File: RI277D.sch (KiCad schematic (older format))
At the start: 8 parts, among them J1 Ribbon Cable, J2 Multiway

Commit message: version 1.2 prototype ready
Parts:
- removed J2: Multiway, Connector_PinHeader_2.54mm:PinHeader_1x06_P2.54mm_Vertical, symbol Connector_Generic:Conn_01x06
- added J2: Tape Return, Connector_Molex:Molex_KK-254_AE-6410-03A_1x03_P2.54mm_Vertical, symbol Connector_Generic:Conn_01x03
- J1: footprint Connector_PinHeader_2.54mm:PinHeader_1x10_P2.54mm_Vertical -> Connector_Molex:Molex_KK-254_AE-6410-10A_1x10_P2.54mm_Vertical
- SK1: footprint Connector_PinHeader_2.54mm:PinHeader_1x03_P2.54mm_Vertical -> Connector_Molex:Molex_KK-254_AE-6410-03A_1x03_P2.54mm_Vertical
- SK2, SK3, SK4: footprint Connector_Audio:Jack_6.35mm_Neutrik_NMJ6HCD2_Horizontal -> Cliff:CL13345
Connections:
- net at J1.1 (Pin_1): now also SK1.3 (Pin_3); no longer SK1.2 (Pin_2)
- net at J1.2 (Pin_2): now also SK1.2 (Pin_2); no longer SK1.3 (Pin_3)
- net at J1.6 (Pin_6), SK2.RN: now also J2.3 (Pin_3)
- net GND: now reaches R2.1, SK1.1 (Pin_1), SK2.S, SK2.SN, SK3.S, SK3.SN, SK4.S, SK4.SN
- net GND: now also J2.1 (Pin_1)
- net at SK2.TN: now also J2.2 (Pin_2)
- no-connect marks 0 -> 5
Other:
- note added: "SCN\nTRR\nTRT\n1 GND\n3 -\n2 +"
- note removed: "SCN\nTRR\nTRT\nSCN\n-\n+"
- moved on the sheet: SK1
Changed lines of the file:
@@
 U 1 1 5F7BCA68
 P 4200 3000
-F 0 "J1" H 4150 3600 50  0000 L CNN
-F 1 "Ribbon Cable" H 4150 3500 50  0000 L CNN
-F 2 "Connector_PinHeader_2.54mm:PinHeader_1x10_P2.54mm_Vertical" H 4200 3000 50  0001 C CNN
+F 0 "J1" H 4150 2400 50  0000 L CNN
+F 1 "Ribbon Cable" H 4300 2400 50  0000 L CNN
+F 2 "Connector_Molex:Molex_KK-254_AE-6410-10A_1x10_P2.54mm_Vertical" H 4200 3000 50  0001 C CNN
 F 3 "~" H 4200 3000 50  0001 C CNN
 	1    4200 3000
@@
 $EndComp
 $Comp
-L Connector_Generic:Conn_01x06 J2
-U 1 1 5F7C4141
-P 4200 2000
-F 0 "J2" H 4150 2400 50  0000 L CNN
-F 1 "Multiway" H 4150 2300 50  0000 L CNN
-F 2 "Connector_PinHeader_2.54mm:PinHeader_1x06_P2.54mm_Vertical" H 4200 2000 50  0001 C CNN
-F 3 "~" H 4200 2000 50  0001 C CNN
-	1    4200 2000
-	1    0    0    -1
-$EndComp
-$Comp
 L Connector_Generic:Conn_01x03 SK1
 U 1 1 5F7C5243
-P 4200 3900
-F 0 "SK1" H 4150 4200 50  0000 L CNN
-F 1 "MIC Input" H 4150 4100 50  0000 L CNN
-F 2 "Connector_PinHeader_2.54mm:PinHeader_1x03_P2.54mm_Vertical" H 4200 3900 50  0001 C CNN
-F 3 "~" H 4200 3900 50  0001 C CNN
-	1    4200 3900
+P 4200 2200
+F 0 "SK1" H 4150 2000 50  0000 L CNN
+F 1 "MIC Input" H 4350 2000 50  0000 L CNN
+F 2 "Connector_Molex:Molex_KK-254_AE-6410-03A_1x03_P2.54mm_Vertical" H 4200 2200 50  0001 C CNN
+F 3 "~" H 4200 2200 50  0001 C CNN
+	1    4200 2200
 	1    0    0    -1
 $EndComp
@@
 Connection ~ 2700 1800
 Wire Wire Line
-	2700 1800 3900 1800
+	2700 1800 3400 1800
 Wire Wire Line
 	2600 3500 2700 3500
@@
 	2700 3800 2800 3800
 Wire Wire Line
-	3600 3900 3600 3500
-Wire Wire Line
-	3600 3500 4000 3500
+	3900 3800 3900 3500
+Wire Wire Line
+	3900 3500 4000 3500
 Wire Wire Line
 	2600 2850 2900 2850
@@
 	3600 1900 4000 1900
 Wire Wire Line
-	4000 2600 3800 2600
-Wire Wire Line
-	3800 2600 3800 2300
-Wire Wire Line
-	3800 2300 4000 2300
-Wire Wire Line
-	4000 3900 3800 3900
-Wire Wire Line
-	3800 3900 3800 2600
-Connection ~ 3800 2600
-Wire Wire Line
-	3700 4000 3700 2700
-Wire Wire Line
-	3700 2200 4000 2200
-Wire Wire Line
-	4000 2700 3700 2700
+	4000 2600 3900 2600
+Wire Wire Line
+	3900 2600 3900 2300
+Wire Wire Line
+	3900 2300 4000 2300
+Wire Wire Line
+	3800 2200 4000 2200
+Wire Wire Line
+	4000 2700 3800 2700
 $Comp
 L Connector:AudioJack3_Switch SK3
@@
 F 0 "SK3" H 2382 3275 50  0000 C CNN
 F 1 "Insert" H 2382 3184 50  0000 C CNN
-F 2 "Connector_Audio:Jack_6.35mm_Neutrik_NMJ6HCD2_Horizontal" H 2400 2850 50  0001 C CNN
+F 2 "Cliff:CL13345" H 2400 2850 50  0001 C CNN
 F 3 "~" H 2400 2850 50  0001 C CNN
 	1    2400 2850
@@
 F 0 "SK4" H 2382 4125 50  0000 C CNN
 F 1 "Direct Out" H 2382 4034 50  0000 C CNN
-F 2 "Connector_Audio:Jack_6.35mm_Neutrik_NMJ6HCD2_Horizontal" H 2400 3700 50  0001 C CNN
+F 2 "Cliff:CL13345" H 2400 3700 50  0001 C CNN
 F 3 "~" H 2400 3700 50  0001 C CNN
 	1    2400 3700
@@
 $EndComp
 Wire Wire Line
-	3700 4000 4000 4000
-Wire Wire Line
 	2600 3900 3200 3900
 Wire Wire Line
-	3100 3800 3200 3800
-Wire Wire Line
-	3200 3800 3200 3900
-Connection ~ 3200 3900
-Wire Wire Line
-	3200 3900 3600 3900
-Wire Wire Line
-	3200 3700 3900 3700
-Wire Wire Line
-	3900 3700 3900 3800
-Wire Wire Line
-	3900 3800 4000 3800
-Connection ~ 3200 3700
-Wire Wire Line
 	2900 2850 2900 3400
-Connection ~ 3700 2700
-Wire Wire Line
-	3700 2200 3700 2700
+Wire Wire Line
+	3800 2200 3800 2700
 $Comp
 L Connector:AudioJack3_Switch SK2
@@
 F 0 "SK2" H 2382 2425 50  0000 C CNN
 F 1 "Line Input" H 2382 2334 50  0000 C CNN
-F 2 "Connector_Audio:Jack_6.35mm_Neutrik_NMJ6HCD2_Horizontal" H 2400 2000 50  0001 C CNN
+F 2 "Cliff:CL13345" H 2400 2000 50  0001 C CNN
 F 3 "~" H 2400 2000 50  0001 C CNN
 	1    2400 2000
@@
 $EndComp
 Text Notes 4300 2350 0    63   ~ 0
-SCN\nTRR\nTRT\nSCN\n-\n+
+SCN\nTRR\nTRT\n1 GND\n3 -\n2 +
+Connection ~ 3400 1800
+Wire Wire Line
+	3400 1800 3900 1800
+$Comp
+L power:GND #PWR0101
+U 1 1 5F984D98
+P 3400 1900
+F 0 "#PWR0101" H 3400 1650 50  0001 C CNN
+F 1 "GND" H 3500 1950 50  0000 C CNN
+F 2 "" H 3400 1900 50  0001 C CNN
+F 3 "" H 3400 1900 50  0001 C CNN
+	1    3400 1900
+	1    0    0    -1
+$EndComp
+Wire Wire Line
+	3400 1900 3400 1800
+$Comp
+L Connector_Generic:Conn_01x03 J2
+U 1 1 5F989AAC
+P 4200 1900
+F 0 "J2" H 4150 2100 50  0000 L CNN
+F 1 "Tape Return" H 4300 2100 50  0000 L CNN
+F 2 "Connector_Molex:Molex_KK-254_AE-6410-03A_1x03_P2.54mm_Vertical" H 4200 1900 50  0001 C CNN
+F 3 "~" H 4200 1900 50  0001 C CNN
+	1    4200 1900
+	1    0    0    -1
+$EndComp
+Wire Wire Line
+	3100 3800 3200 3800
+Wire Wire Line
+	3200 3900 3200 3800
+Connection ~ 3200 3800
+Wire Wire Line
+	3200 3800 3900 3800
+NoConn ~ 2600 3150
+NoConn ~ 2600 3800
+NoConn ~ 2600 4000
+NoConn ~ 4000 3200
+NoConn ~ 4000 2800
 $EndSCHEMATC

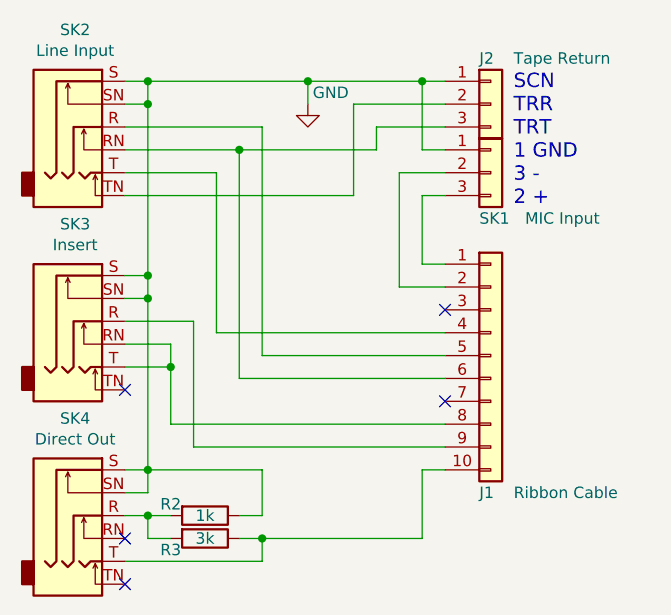
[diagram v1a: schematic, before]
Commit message: added git submodule library and wirebridge to layout
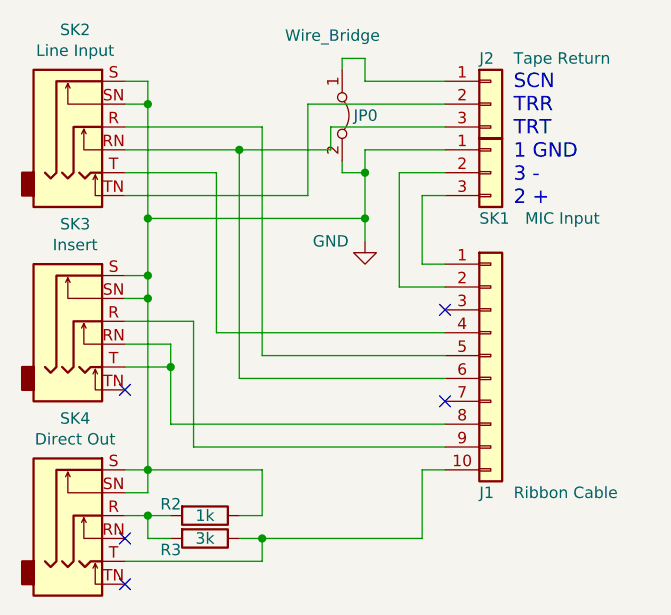
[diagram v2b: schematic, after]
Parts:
- added JP0: Wire_Bridge, TAC:Wire_Bridge_P10.16mm_Horizontal, symbol Jumper:Jumper_2_Bridged
- SK2, SK3, SK4: footprint Cliff:CL13345 -> TAC:CL13345
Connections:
- net GND: now also JP0.2 (B); no longer J2.1 (Pin_1)
- new net: J2.1 (Pin_1), JP0.1 (A)
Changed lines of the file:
@@
 Wire Wire Line
 	2600 2650 2700 2650
-Connection ~ 2700 1800
-Wire Wire Line
-	2700 1800 3400 1800
 Wire Wire Line
 	2600 3500 2700 3500
@@
 Wire Wire Line
 	2700 1800 2700 1900
-Wire Wire Line
-	4000 2100 3900 2100
-Wire Wire Line
-	3900 2100 3900 1800
-Connection ~ 3900 1800
-Wire Wire Line
-	3900 1800 4000 1800
 $Comp
 L Device:R R2
@@
 Connection ~ 2700 1900
 Wire Wire Line
-	2700 1900 2700 2650
-Wire Wire Line
 	2600 2750 2700 2750
 Connection ~ 2700 2750
@@
 	3100 3100 4000 3100
 Wire Wire Line
-	4000 2000 3700 2000
-Wire Wire Line
-	3700 2000 3700 2100
-Wire Wire Line
-	3700 2100 3100 2100
+	4000 2000 3500 2000
+Wire Wire Line
+	3500 2000 3500 2100
+Wire Wire Line
+	3500 2100 3100 2100
 Connection ~ 3100 2100
 Wire Wire Line
-	2600 2300 3600 2300
-Wire Wire Line
-	3600 2300 3600 1900
-Wire Wire Line
-	3600 1900 4000 1900
+	2600 2300 3400 2300
+Wire Wire Line
+	3400 2300 3400 1900
+Wire Wire Line
+	3400 1900 4000 1900
 Wire Wire Line
 	4000 2600 3900 2600
@@
 F 0 "SK3" H 2382 3275 50  0000 C CNN
 F 1 "Insert" H 2382 3184 50  0000 C CNN
-F 2 "Cliff:CL13345" H 2400 2850 50  0001 C CNN
+F 2 "TAC:CL13345" H 2400 2850 50  0001 C CNN
 F 3 "~" H 2400 2850 50  0001 C CNN
 	1    2400 2850
@@
 F 0 "SK4" H 2382 4125 50  0000 C CNN
 F 1 "Direct Out" H 2382 4034 50  0000 C CNN
-F 2 "Cliff:CL13345" H 2400 3700 50  0001 C CNN
+F 2 "TAC:CL13345" H 2400 3700 50  0001 C CNN
 F 3 "~" H 2400 3700 50  0001 C CNN
 	1    2400 3700
@@
 F 0 "SK2" H 2382 2425 50  0000 C CNN
 F 1 "Line Input" H 2382 2334 50  0000 C CNN
-F 2 "Cliff:CL13345" H 2400 2000 50  0001 C CNN
+F 2 "TAC:CL13345" H 2400 2000 50  0001 C CNN
 F 3 "~" H 2400 2000 50  0001 C CNN
 	1    2400 2000
@@
 Text Notes 4300 2350 0    63   ~ 0
 SCN\nTRR\nTRT\n1 GND\n3 -\n2 +
-Connection ~ 3400 1800
-Wire Wire Line
-	3400 1800 3900 1800
-$Comp
-L power:GND #PWR0101
-U 1 1 5F984D98
-P 3400 1900
-F 0 "#PWR0101" H 3400 1650 50  0001 C CNN
-F 1 "GND" H 3500 1950 50  0000 C CNN
-F 2 "" H 3400 1900 50  0001 C CNN
-F 3 "" H 3400 1900 50  0001 C CNN
-	1    3400 1900
-	1    0    0    -1
-$EndComp
-Wire Wire Line
-	3400 1900 3400 1800
 $Comp
 L Connector_Generic:Conn_01x03 J2
@@
 NoConn ~ 4000 3200
 NoConn ~ 4000 2800
+Wire Wire Line
+	2700 1900 2700 2400
+$Comp
+L power:GND #PWR0101
+U 1 1 5F984D98
+P 3650 2500
+F 0 "#PWR0101" H 3650 2250 50  0001 C CNN
+F 1 "GND" H 3500 2500 50  0000 C CNN
+F 2 "" H 3650 2500 50  0001 C CNN
+F 3 "" H 3650 2500 50  0001 C CNN
+	1    3650 2500
+	1    0    0    -1
+$EndComp
+Wire Wire Line
+	4000 2100 3650 2100
+$Comp
+L Jumper:Jumper_2_Bridged JP0
+U 1 1 5FC705CE
+P 3550 1950
+F 0 "JP0" V 3550 2000 50  0000 L CNN
+F 1 "Wire_Bridge" V 3200 1700 50  0000 L CNN
+F 2 "TAC:Wire_Bridge_P10.16mm_Horizontal" H 3550 1950 50  0001 C CNN
+F 3 "~" H 3550 1950 50  0001 C CNN
+	1    3550 1950
+	0    1    1    0
+$EndComp
+Wire Wire Line
+	3550 2200 3650 2200
+Wire Wire Line
+	3650 2200 3650 2100
+Wire Wire Line
+	3650 2200 3650 2400
+Connection ~ 3650 2200
+Wire Wire Line
+	3650 2400 2700 2400
+Connection ~ 3650 2400
+Wire Wire Line
+	3650 2400 3650 2500
+Connection ~ 2700 2400
+Wire Wire Line
+	2700 2400 2700 2650
+Wire Wire Line
+	3550 1750 3550 1700
+Wire Wire Line
+	3650 1700 3650 1800
+Wire Wire Line
+	3650 1800 4000 1800
+Wire Wire Line
+	3550 1700 3650 1700
+Wire Wire Line
+	3550 2200 3550 2150
 $EndSCHEMATC
